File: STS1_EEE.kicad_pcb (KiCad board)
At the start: 4 copper layers, 81.1 x 85 mm, 43 parts, among them J1 Conn_02x20_Odd_Even, J2 Conn_02x20_Odd_Even, SW1 SW_SPST, U1 coordinate_system, U2 ST_Logo, U3 MP28167GQ, U4 1047

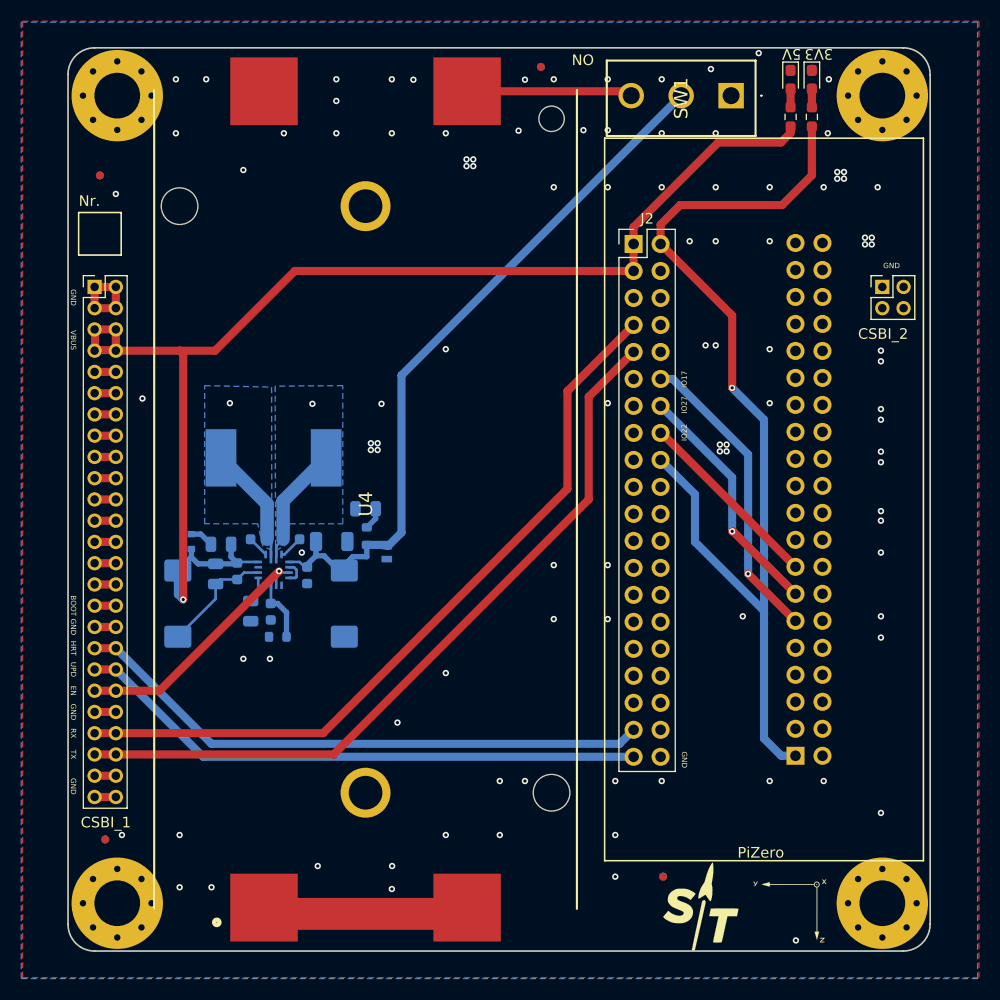
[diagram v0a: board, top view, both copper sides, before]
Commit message: Replace batter holder: 1048P -> 1049
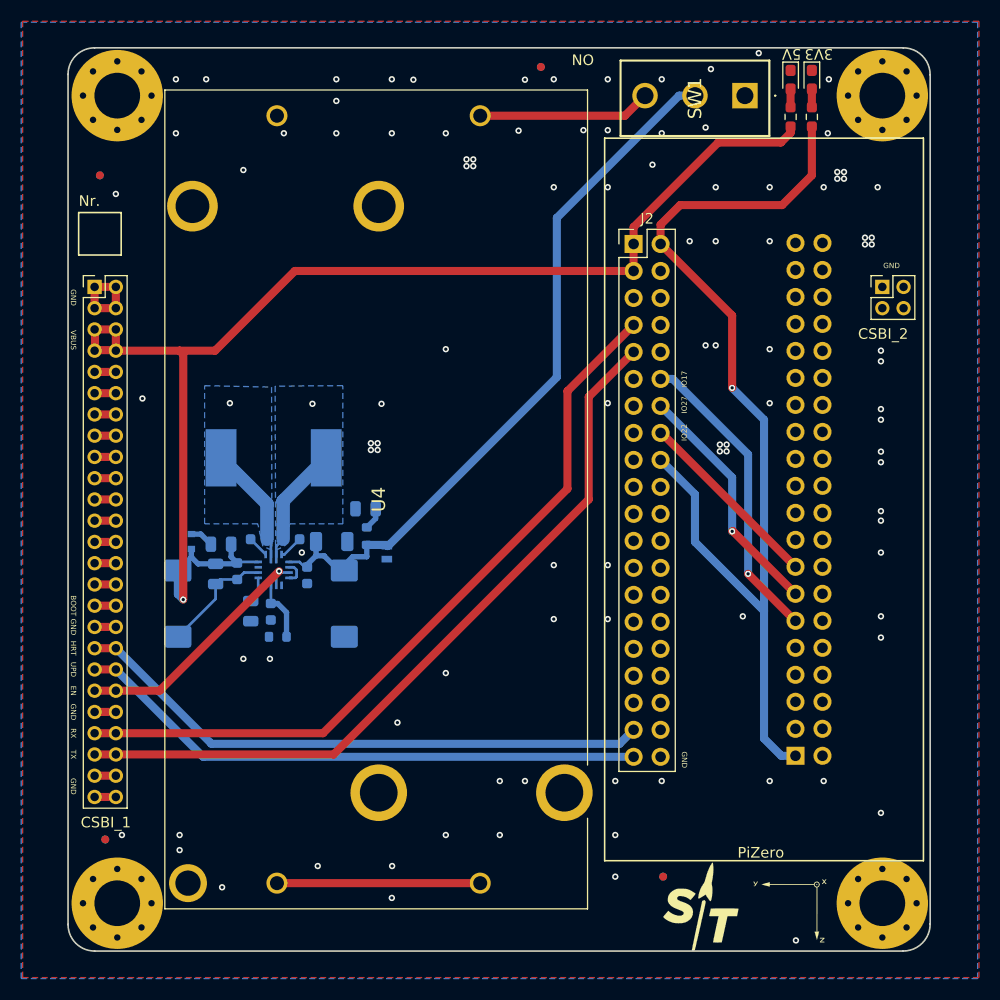
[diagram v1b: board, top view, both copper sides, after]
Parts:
- U4: value 1047 -> 1049; footprint STS_EEE:1048P -> STS_EEE:1049
- moved SW1 1.30 mm to (179.7, 46.3)
- moved U4 1.00 mm to (145.0, 84.3), turned to -90 degrees
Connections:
- U4 pad 1: Net-(U4-Pad1) -> unconnected-(U4-Pad1)
- U4 pad 2: Net-(U4-Pad1) -> unconnected-(U4-Pad2)
- U4 pad 3: Net-(SW1-NO) -> unconnected-(U4-Pad3)
- U4 pad 4: GND -> unconnected-(U4-Pad4)
- U4 pad 6: (no net) -> GND
- U4 pad 7: (no net) -> Net-(SW1-NO)
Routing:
- net Net-(U4-Pad8): track 0.00 -> 19.1 mm
- net VBAT: track 67.9 -> 69.3 mm

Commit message: Fix missing GND pin connection of U3
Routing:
- net GND: track 35.3 -> 37.0 mm
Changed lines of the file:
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@@
+	)
+	(segment
+		(start 134.127532 91.183216)
+		(end 133.898932 91.183216)
+		(width 0.2032)
+		(layer "B.Cu")
+		(net "GND")
+	)
+	(segment
+		(start 134.59887 91.654554)
+		(end 134.127532 91.183216)
+		(width 0.2032)
+		(layer "B.Cu")
+		(net "GND")
 	)
 	(segment
@@
 		(end 129.890932 92.260805)
 		(width 0.254)
+		(layer "B.Cu")
+		(net "GND")
+	)
+	(segment
+		(start 134.59887 92.383302)
+		(end 134.59887 91.654554)
+		(width 0.2032)
 		(layer "B.Cu")
 		(net "GND")
@@
 	)
 	(segment
+		(start 135.66 120.41)
+		(end 154.79 120.41)
+		(width 0.762)
+		(layer "F.Cu")
+		(net "Net-(U4-Pad8)")
+	)
+	(segment
 		(start 146.1125 88.6875)
 		(end 162 72.8)
@@
 		(net "Net-(U3-BST2)")
 	)
-	(segment
-		(start 135.66 120.41)
-		(end 154.79 120.41)
-		(width 0.762)
-		(layer "F.Cu")
-		(net "Net-(U4-Pad8)")
-	)
 	(zone

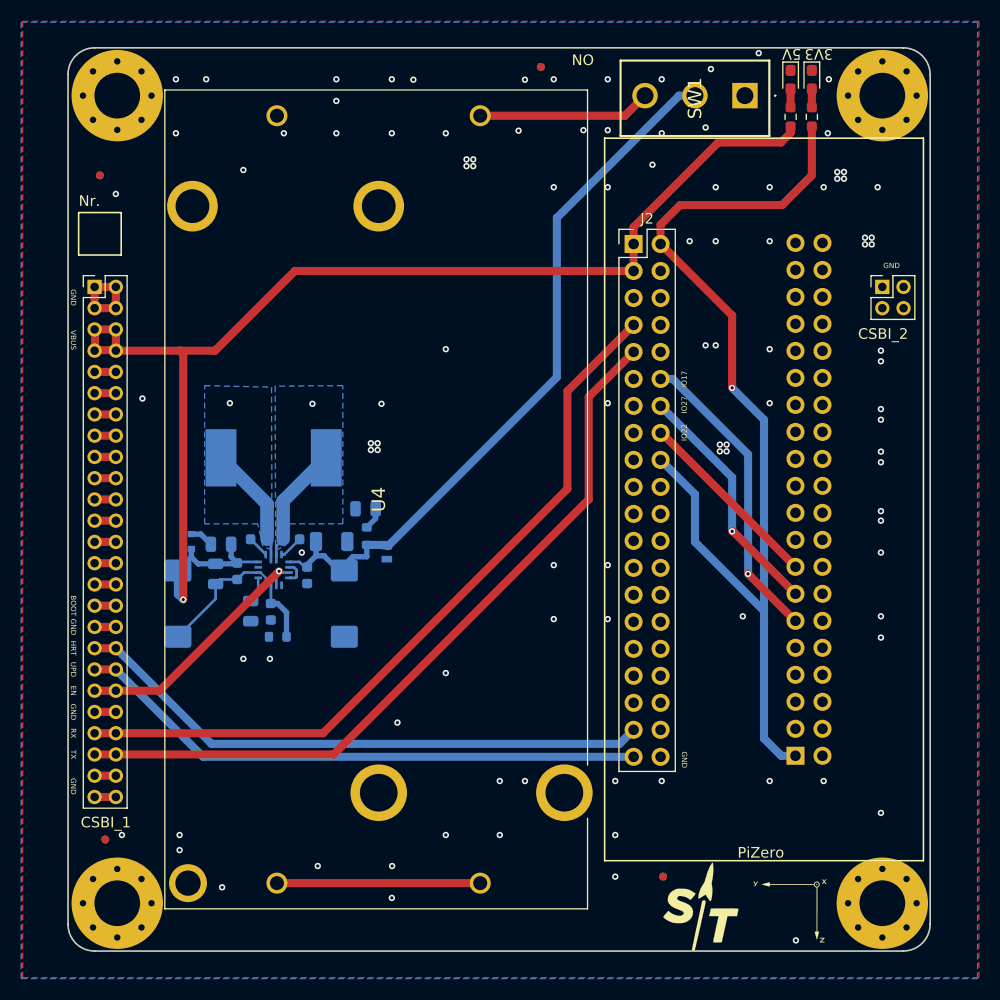
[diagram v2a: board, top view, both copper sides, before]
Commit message: Fix some of the DRC warnings
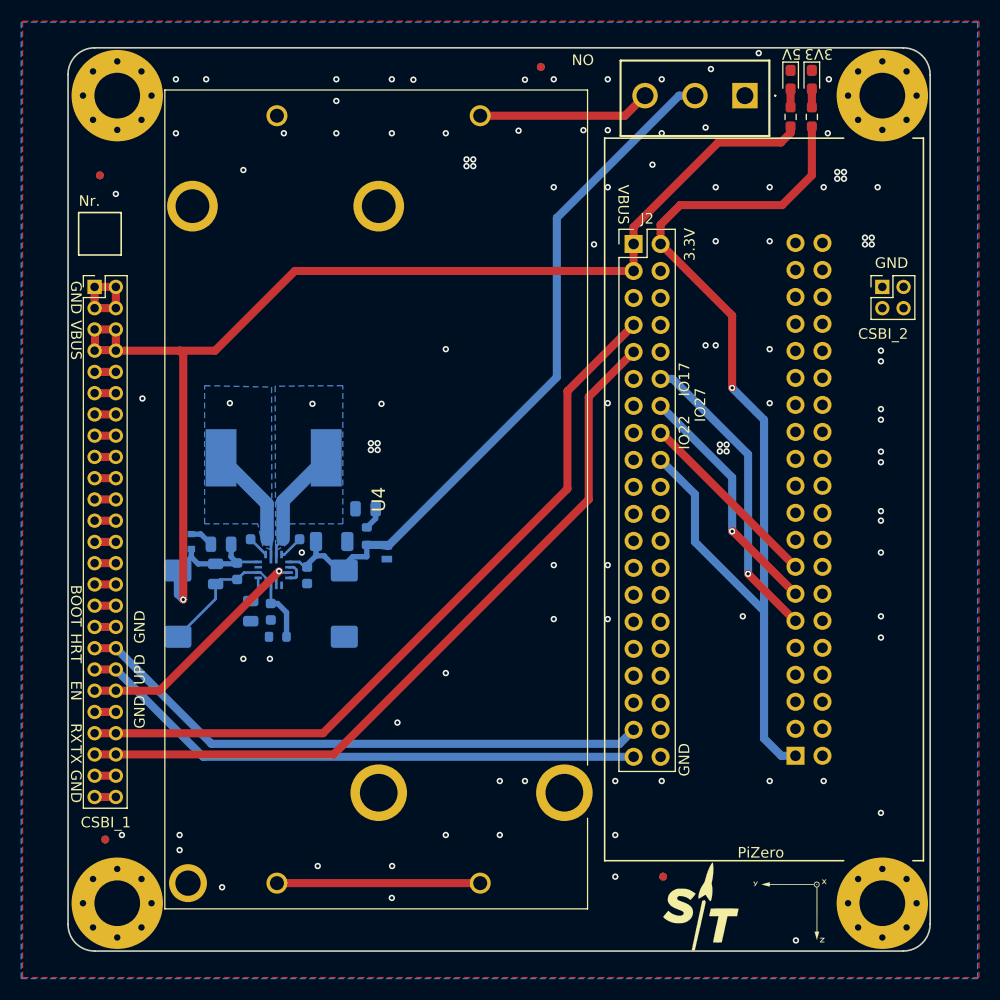
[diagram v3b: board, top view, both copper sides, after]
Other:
- board text added: "3.3V"
